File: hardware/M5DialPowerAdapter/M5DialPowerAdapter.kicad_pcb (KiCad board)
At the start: 2 copper layers, 35.4 x 46.8 mm, 15 parts, among them J1 Power In, J2 LED Power, J3 M5Dial Power, J4 JST XH I2C, J5 Grove I2C, U1 AMS1117-3.3

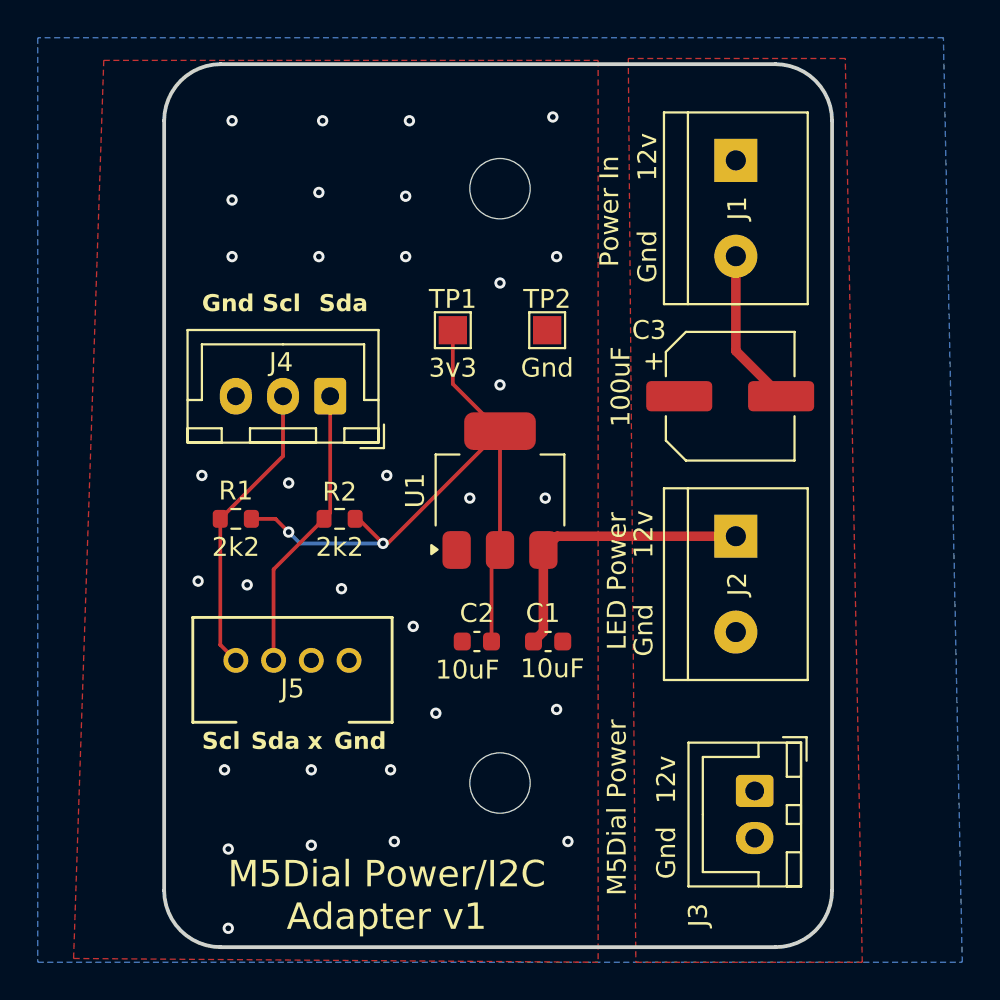
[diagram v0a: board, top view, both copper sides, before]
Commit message: Updates to bring 12 volts from Caddy
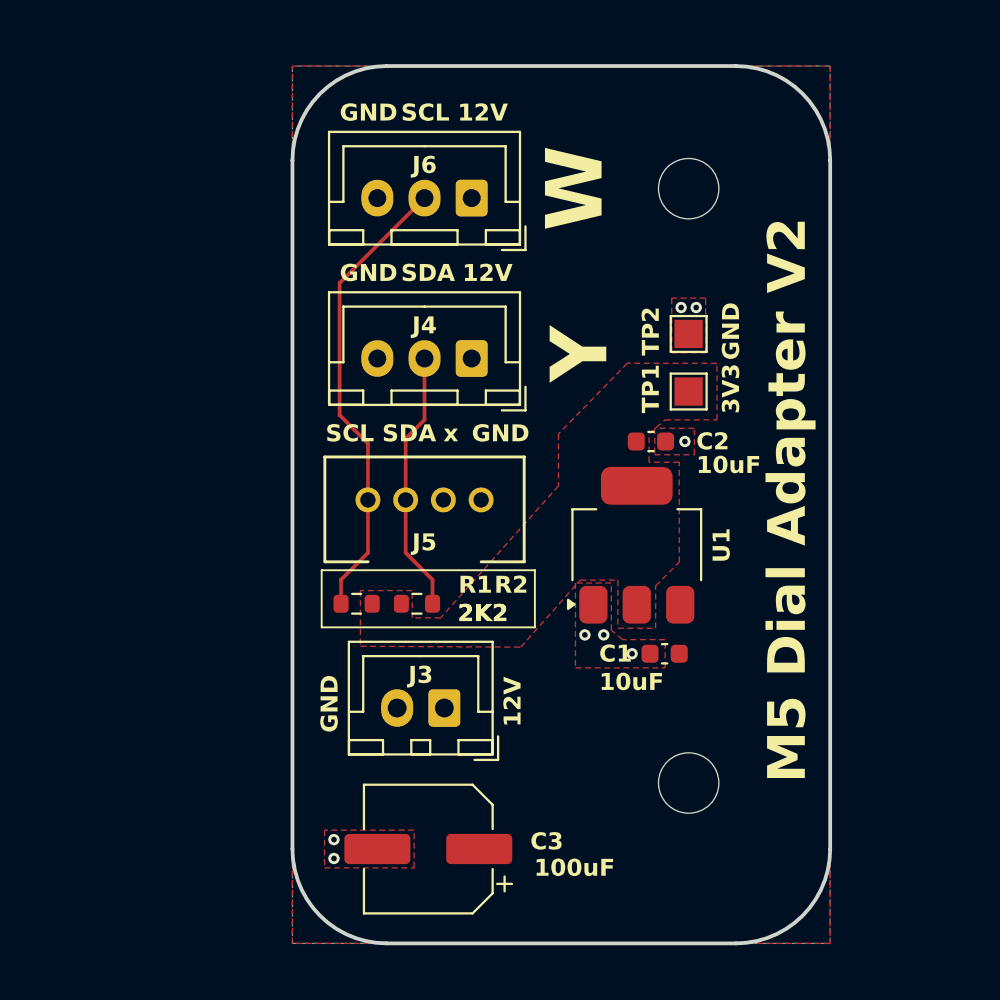
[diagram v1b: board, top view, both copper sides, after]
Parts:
- removed J1: Power In, Useful Modifications:TerminalBlock_bornier-2_P5.08mm
- removed J2: LED Power, Useful Modifications:TerminalBlock_bornier-2_P5.08mm
- added J6: JST XH SCL, Connector_JST:JST_XH_B3B-XH-A_1x03_P2.50mm_Vertical, F.Cu at (148.5, 60.5)
- J4: value JST XH I2C -> JST XH SCA
- R1, R2: value 2k2 -> 2K2
- TP1: value 3v3 -> 3V3
- TP2: value Gnd -> GND
- moved C3 28.8 mm to (146.2, 95.0), turned to 180 degrees
- moved J3 17.0 mm to (147.1, 87.5), turned to 180 degrees
- moved C2 14.1 mm to (158.0, 73.4), turned to 0 degrees
- moved TP1 12.9 mm to (160.0, 70.8)
- moved J5 11.0 mm to (143.0, 76.5)
- moved H1 10.0 mm to (160.0, 60.0)
- moved H2 10.0 mm to (160.0, 91.5)
- moved R1 7.82 mm to (142.4, 82.0)
- moved U1 7.81 mm to (157.2, 78.9)
- moved J4 7.76 mm to (148.5, 69.0)
- moved TP2 7.50 mm to (160.0, 67.7)
- moved C1 6.21 mm to (158.7, 84.7), turned to 180 degrees
- moved R2 6.09 mm to (145.6, 82.0), turned to 180 degrees
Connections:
- J4 pad 1: SDA -> +12V
- J4 pad 2: SCL -> SDA
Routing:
- net +3V3: track 35.9 -> 0.00 mm, vias 2 -> 0
- net +12V: track 15.6 -> 0.00 mm
- net SCL: track 15.7 -> 24.6 mm
- net GND: track 8.41 -> 0.00 mm, vias 32 -> 8
- net SDA: track 15.2 -> 14.0 mm
- added copper zone on F.Cu, net +3V3
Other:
- board size 35.4 x 46.8 mm -> 28.5 x 46.5 mm
- board text added: "12V"
- board text added: "GND"
- board text added: "M5 Dial Adapter V2"
- board text added: "SCL"
- board text added: "SDA"
- board text added: "W"
- board text added: "Y"
- board text removed: "12v"
- board text removed: "Gnd"
- board text removed: "M5Dial Power/I2C Adapter v1"
- board text removed: "Scl"
- board text removed: "Sda"
